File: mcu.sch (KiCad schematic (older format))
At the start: 15 parts, among them U17 STM32F407VETx, Y1 Crystal_Small

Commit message: Transformation will begin shortly... ;-)
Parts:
- added C17: 100n, Capacitors_SMD:C_1206_HandSoldering, symbol C_Small
- added D5: LED.RED, LEDs:LED_1206, symbol Led_Small
- added J1: Micro_SD_Card_Det, RetroBitLab:microSD_HC_Hirose_DM3D-SF, symbol Micro_SD_Card_Det
- added R10, R20: 220, Resistors_SMD:R_1206_HandSoldering, symbol R_Small
- added R11, R12: 10k, Resistors_SMD:R_1206_HandSoldering, symbol R_Small
- added R13, R14, R15, R16, R17, R19: 0, Resistors_SMD:R_1206_HandSoldering, symbol R_Small
- added R18: 47k, Resistors_SMD:R_1206_HandSoldering, symbol R_Small
- C14, C15, C16, C6, C7, C8, C9: footprint (none) -> Capacitors_SMD:C_1206_HandSoldering
- C4, C5: value C_Small -> 20p; footprint (none) -> Capacitors_SMD:C_1206_HandSoldering
- D3: value Led_Small -> LED.GREEN; footprint (none) -> LEDs:LED_1206
- D4: value Led_Small -> LED.AMBER; footprint (none) -> LEDs:LED_1206
- R4, R5: footprint (none) -> Resistors_SMD:R_1206_HandSoldering
- U17: footprint Package_QFP:LQFP-100_14x14mm_P0.5mm -> Housings_QFP:LQFP-100_14x14mm_Pitch0.5mm
- Y1: value Crystal_Small -> 8Mhz; footprint (none) -> Crystal:Crystal_SMD_0603-4Pin_6.0x3.5mm_HandSoldering
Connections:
- net GND: now also C17.2, D5.1 (K), J1.6 (VSS), R13.1, R14.1, R15.1, R16.1, R17.1
- net VCC3V3: now also C17.1, J1.4 (VDD), R11.1, R12.1, R18.1
- net mSDCLK: now also J1.5 (CLK)
- net mSDI: now also J1.3 (CMD)
- net mSDO: now also J1.7 (DAT0), R18.2
- net mD1E0_A10: now reaches U17.1 (PE2)
- net at C4.1, Y1.1: now also R19.2; no longer U17.12 (PH0)
- net at C5.1, Y1.2: now also R20.2; no longer U17.13 (PH1)
- net TP1: now reaches U17.18 (PC3)
- net mD1E0_A11: now reaches U17.2 (PE3)
- net mD1E0_A12: now reaches U17.3 (PE4)
- net LEDGRN: now reaches R4.2, U17.35 (PB0)
- net LEDAMBER: now reaches R5.2
- net LEDAMBER: now also U17.89 (PB3); no longer U17.36 (PB1)
- net mD1E0_A15: now reaches U17.38 (PE7)
- net mD1E0_A13: now reaches U17.4 (PE5)
- net SPARE1: now reaches U17.47 (PB10)
- net SPARE1: now also R13.2
- net SPARE2: now reaches U17.48 (PB11)
- net SPARE2: now also R14.2
- net mD1E0_A14: now reaches U17.5 (PE6)
- net SPARE3: now reaches U17.51 (PB12)
- net SPARE3: now also R15.2
- net SPARE4: now reaches U17.63 (PC6)
- net SPARE4: now also R16.2
- net SPARE5: now reaches U17.64 (PC7)
- net SPARE5: now also R17.2
- net mD1E2_A16: now reaches U17.65 (PC8)
- net mD1E2_A17: now reaches U17.66 (PC9)
- net ~mIRQ: now reaches U17.67 (PA8)
- net UART_TX_TTL: now reaches U17.68 (PA9)
- net UART_TX_TTL: now also R12.2
- net UART_RX_TTL: now reaches U17.69 (PA10)
- net UART_RX_TTL: now also R11.2
- net mD1E3_A21: now reaches U17.7 (PC13)
- net ~mREF: now reaches U17.70 (PA11)
- net ~mD3XX: now reaches U17.71 (PA12)
- net SWDIO: now reaches U17.72 (PA13)
- net SWDCLK: now reaches U17.76 (PA14)
- net RAMEN: now reaches U17.77 (PA15)
- net mD1E2_A18: now reaches U17.78 (PC10)
- net mD1E2_A19: now reaches U17.79 (PC11)
- net mD1E3_A20: now reaches U17.80 (PC12)
- net mRD4: now reaches U17.90 (PB4)
- net mD1E0_A8: now reaches U17.97 (PE0)
- net mD1E0_A9: now reaches U17.98 (PE1)
- net mBO2/PHI2 renamed mB02/PHI2
- net nRST renamed nRESET
- new net: R19.1, U17.12 (PH0)
- new net: R20.1, U17.13 (PH1)
- new net: D5.2 (A), R10.1
- new net LEDRED: R10.2, U17.36 (PB1)
- no-connect marks 3 -> 19
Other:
- note added: "AMBER LED (MEMORY ACCESS SRAM)"
- note added: "GREEN LED (CARTRIDGE SWITCHING)"
- note added: "MICROSD Card Connector in SPI MODE"
- note added: "RED LED (BOARD OK)"
- moved on the sheet: D3, D4, R4, R5

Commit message: Heavily modified. Now it sports a 1024/2048k MIO Ram Expansion and a UNO Cart
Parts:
- renumbered C17 to C10, C6 to C11, C7 to C12, C8 to C13, C9 to C14, C14 to C15, C15 to C16, C16 to C17, C4 to C8, C5 to C9, D5 to D4, D4 to D5, R18 to R10, R4 to R18, R10 to R19, R5 to R20, R19 to R8, R20 to R9, Y1 to XT1
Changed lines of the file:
@@
 VCC3V3
 $Comp
-L Crystal_Small Y1
+L Crystal_Small XT1
 U 1 1 5C421B52
 P 2500 2700
-F 0 "Y1" H 2500 2800 50  0000 C CNN
+F 0 "XT1" H 2500 2800 50  0000 C CNN
 F 1 "8Mhz" H 2500 2600 50  0000 C CNN
 F 2 "Crystal:Crystal_SMD_0603-4Pin_6.0x3.5mm_HandSoldering" H 2500 2700 50  0001 C CNN
@@
 $EndComp
 $Comp
-L C_Small C4
+L C_Small C8
 U 1 1 5C421C91
 P 2100 2350
-F 0 "C4" H 2110 2420 50  0000 L CNN
+F 0 "C8" H 2110 2420 50  0000 L CNN
 F 1 "20p" H 2110 2270 50  0000 L CNN
 F 2 "Capacitors_SMD:C_1206_HandSoldering" H 2100 2350 50  0001 C CNN
@@
 $EndComp
 $Comp
-L C_Small C5
+L C_Small C9
 U 1 1 5C421D1B
 P 2100 3050
-F 0 "C5" H 2110 3120 50  0000 L CNN
+F 0 "C9" H 2110 3120 50  0000 L CNN
 F 1 "20p" H 2110 2970 50  0000 L CNN
 F 2 "Capacitors_SMD:C_1206_HandSoldering" H 2100 3050 50  0001 C CNN
@@
 $EndComp
 $Comp
-L C_Small C6
+L C_Small C11
 U 1 1 5C421E29
 P 8600 850
-F 0 "C6" H 8610 920 50  0000 L CNN
+F 0 "C11" H 8610 920 50  0000 L CNN
 F 1 "100n" H 8610 770 50  0000 L CNN
 F 2 "Capacitors_SMD:C_1206_HandSoldering" H 8600 850 50  0001 C CNN
@@
 $EndComp
 $Comp
-L C_Small C7
+L C_Small C12
 U 1 1 5C421EE5
 P 8600 1200
-F 0 "C7" H 8610 1270 50  0000 L CNN
+F 0 "C12" H 8610 1270 50  0000 L CNN
 F 1 "100n" H 8610 1120 50  0000 L CNN
 F 2 "Capacitors_SMD:C_1206_HandSoldering" H 8600 1200 50  0001 C CNN
@@
 $EndComp
 $Comp
-L C_Small C8
+L C_Small C13
 U 1 1 5C421F19
 P 8600 1550
-F 0 "C8" H 8610 1620 50  0000 L CNN
+F 0 "C13" H 8610 1620 50  0000 L CNN
 F 1 "100n" H 8610 1470 50  0000 L CNN
 F 2 "Capacitors_SMD:C_1206_HandSoldering" H 8600 1550 50  0001 C CNN
@@
 $EndComp
 $Comp
-L C_Small C9
+L C_Small C14
 U 1 1 5C421F4C
 P 8600 1900
-F 0 "C9" H 8610 1970 50  0000 L CNN
+F 0 "C14" H 8610 1970 50  0000 L CNN
 F 1 "100n" H 8610 1820 50  0000 L CNN
 F 2 "Capacitors_SMD:C_1206_HandSoldering" H 8600 1900 50  0001 C CNN
@@
 $EndComp
 $Comp
-L C_Small C14
+L C_Small C15
 U 1 1 5C421F82
 P 8600 2250
-F 0 "C14" H 8610 2320 50  0000 L CNN
+F 0 "C15" H 8610 2320 50  0000 L CNN
 F 1 "100n" H 8610 2170 50  0000 L CNN
 F 2 "Capacitors_SMD:C_1206_HandSoldering" H 8600 2250 50  0001 C CNN
@@
 $EndComp
 $Comp
-L C_Small C15
+L C_Small C16
 U 1 1 5C421FB7
 P 8600 2600
-F 0 "C15" H 8610 2670 50  0000 L CNN
+F 0 "C16" H 8610 2670 50  0000 L CNN
 F 1 "100n" H 8610 2520 50  0000 L CNN
 F 2 "Capacitors_SMD:C_1206_HandSoldering" H 8600 2600 50  0001 C CNN
@@
 $EndComp
 $Comp
-L C_Small C16
+L C_Small C17
 U 1 1 5C421FF7
 P 8600 2950
-F 0 "C16" H 8610 3020 50  0000 L CNN
+F 0 "C17" H 8610 3020 50  0000 L CNN
 F 1 "100n" H 8610 2870 50  0000 L CNN
 F 2 "Capacitors_SMD:C_1206_HandSoldering" H 8600 2950 50  0001 C CNN
@@
 ~mD1XX
 $Comp
-L R_Small R4
+L R_Small R18
 U 1 1 5C422FC6
 P 9950 3850
-F 0 "R4" H 9980 3870 50  0000 L CNN
+F 0 "R18" H 9980 3870 50  0000 L CNN
 F 1 "220" H 9980 3810 50  0000 L CNN
 F 2 "Resistors_SMD:R_1206_HandSoldering" H 9950 3850 50  0001 C CNN
@@
 $EndComp
 $Comp
-L R_Small R5
+L R_Small R20
 U 1 1 5C42306F
 P 10650 3850
-F 0 "R5" H 10680 3870 50  0000 L CNN
+F 0 "R20" H 10680 3870 50  0000 L CNN
 F 1 "220" H 10680 3810 50  0000 L CNN
 F 2 "Resistors_SMD:R_1206_HandSoldering" H 10650 3850 50  0001 C CNN
@@
 $EndComp
 $Comp
-L Led_Small D4
+L Led_Small D5
 U 1 1 5C4231C2
 P 10650 3650
-F 0 "D4" H 10600 3775 50  0000 L CNN
+F 0 "D5" H 10600 3775 50  0000 L CNN
 F 1 "LED.AMBER" H 10475 3550 50  0000 L CNN
 F 2 "LEDs:LED_1206" V 10650 3650 50  0001 C CNN
@@
 mRD4
 $Comp
-L R_Small R10
+L R_Small R19
 U 1 1 5C4340D0
 P 10300 3850
-F 0 "R10" H 10330 3870 50  0000 L CNN
+F 0 "R19" H 10330 3870 50  0000 L CNN
 F 1 "220" H 10330 3810 50  0000 L CNN
 F 2 "Resistors_SMD:R_1206_HandSoldering" H 10300 3850 50  0001 C CNN
@@
 $EndComp
 $Comp
-L Led_Small D5
+L Led_Small D4
 U 1 1 5C4340D8
 P 10300 3650
-F 0 "D5" H 10250 3775 50  0000 L CNN
+F 0 "D4" H 10250 3775 50  0000 L CNN
 F 1 "LED.RED" H 10125 3550 50  0000 L CNN
 F 2 "LEDs:LED_1206" V 10300 3650 50  0001 C CNN
@@
 mSDI
 $Comp
-L R_Small R18
+L R_Small R10
 U 1 1 5C4392C7
 P 2900 4250
-F 0 "R18" H 2700 4250 50  0000 L CNN
+F 0 "R10" H 2700 4250 50  0000 L CNN
 F 1 "47k" H 2950 4250 50  0000 L CNN
 F 2 "Resistors_SMD:R_1206_HandSoldering" H 2900 4250 50  0001 C CNN
@@
 	2400 4450 3150 4450
 $Comp
-L C_Small C17
+L C_Small C10
 U 1 1 5C43AFC5
 P 3500 4950
-F 0 "C17" H 3510 5020 50  0000 L CNN
+F 0 "C10" H 3510 5020 50  0000 L CNN
 F 1 "100n" H 3510 4870 50  0000 L CNN
 F 2 "Capacitors_SMD:C_1206_HandSoldering" H 3500 4950 50  0001 C CNN
@@
 ~mIRQ
 $Comp
-L R_Small R20
+L R_Small R9
 U 1 1 5C43FC39
 P 2850 3050
-F 0 "R20" H 2880 3070 50  0000 L CNN
+F 0 "R9" H 2880 3070 50  0000 L CNN
 F 1 "220" H 2880 3010 50  0000 L CNN
 F 2 "Resistors_SMD:R_1206_HandSoldering" H 2850 3050 50  0001 C CNN
@@
 $EndComp
 $Comp
-L R_Small R19
+L R_Small R8
 U 1 1 5C43FCB0
 P 2850 2350
-F 0 "R19" H 2880 2370 50  0000 L CNN
+F 0 "R8" H 2880 2370 50  0000 L CNN
 F 1 "0" H 2880 2310 50  0000 L CNN
 F 2 "Resistors_SMD:R_1206_HandSoldering" H 2850 2350 50  0001 C CNN

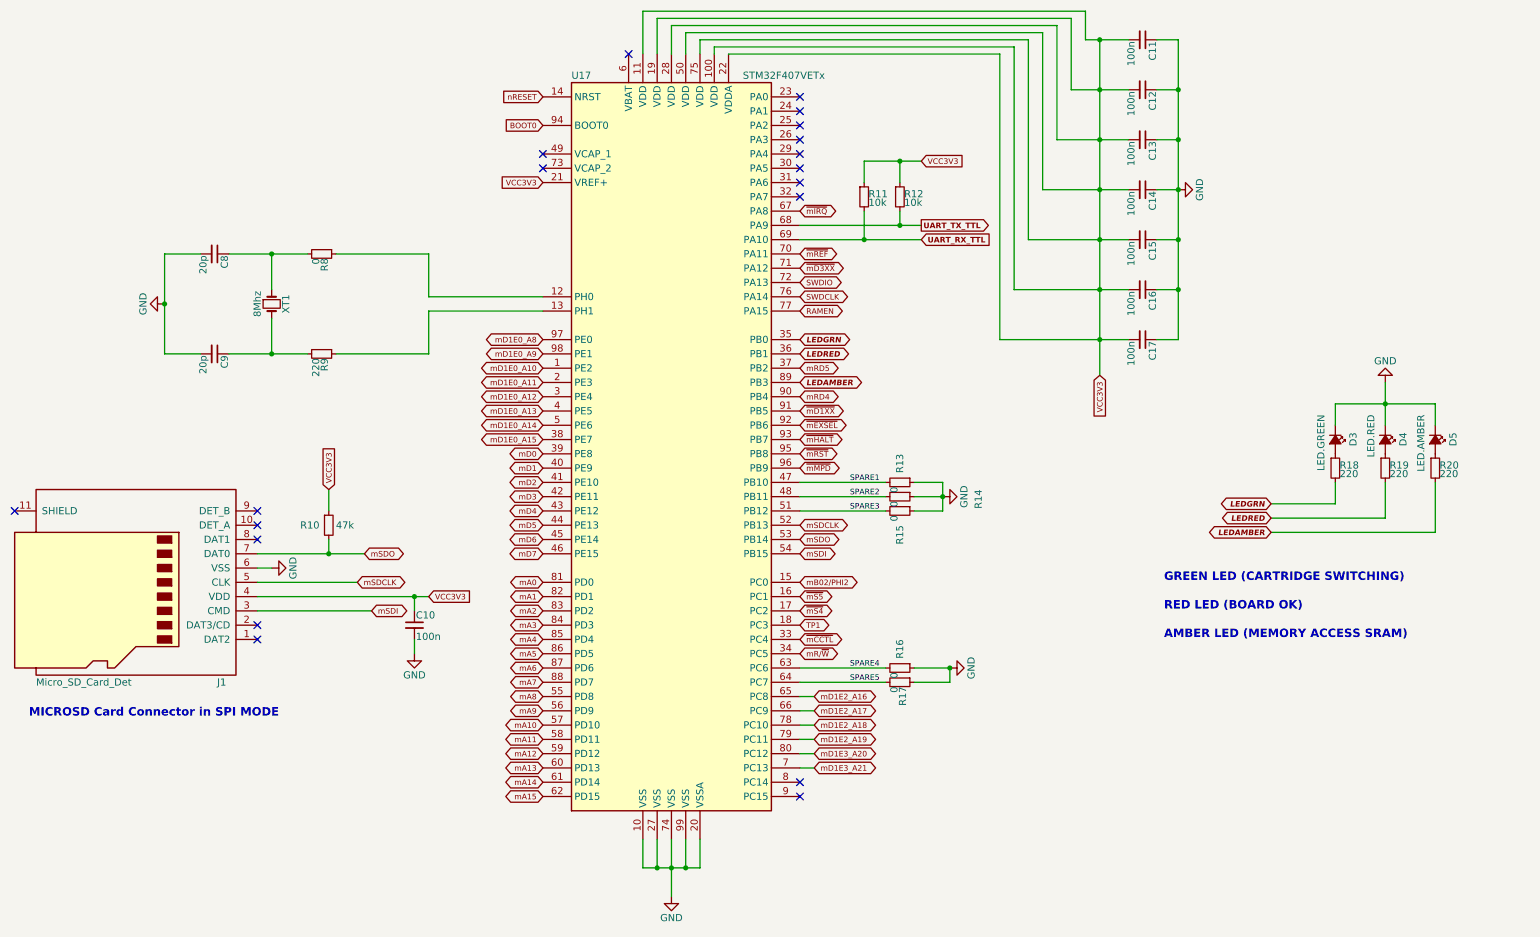
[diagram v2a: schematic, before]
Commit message: Upgraded with the latest infos
Now there is no logic for address/decoding. All is done inside the
microprocessor. This is a semi-final release.
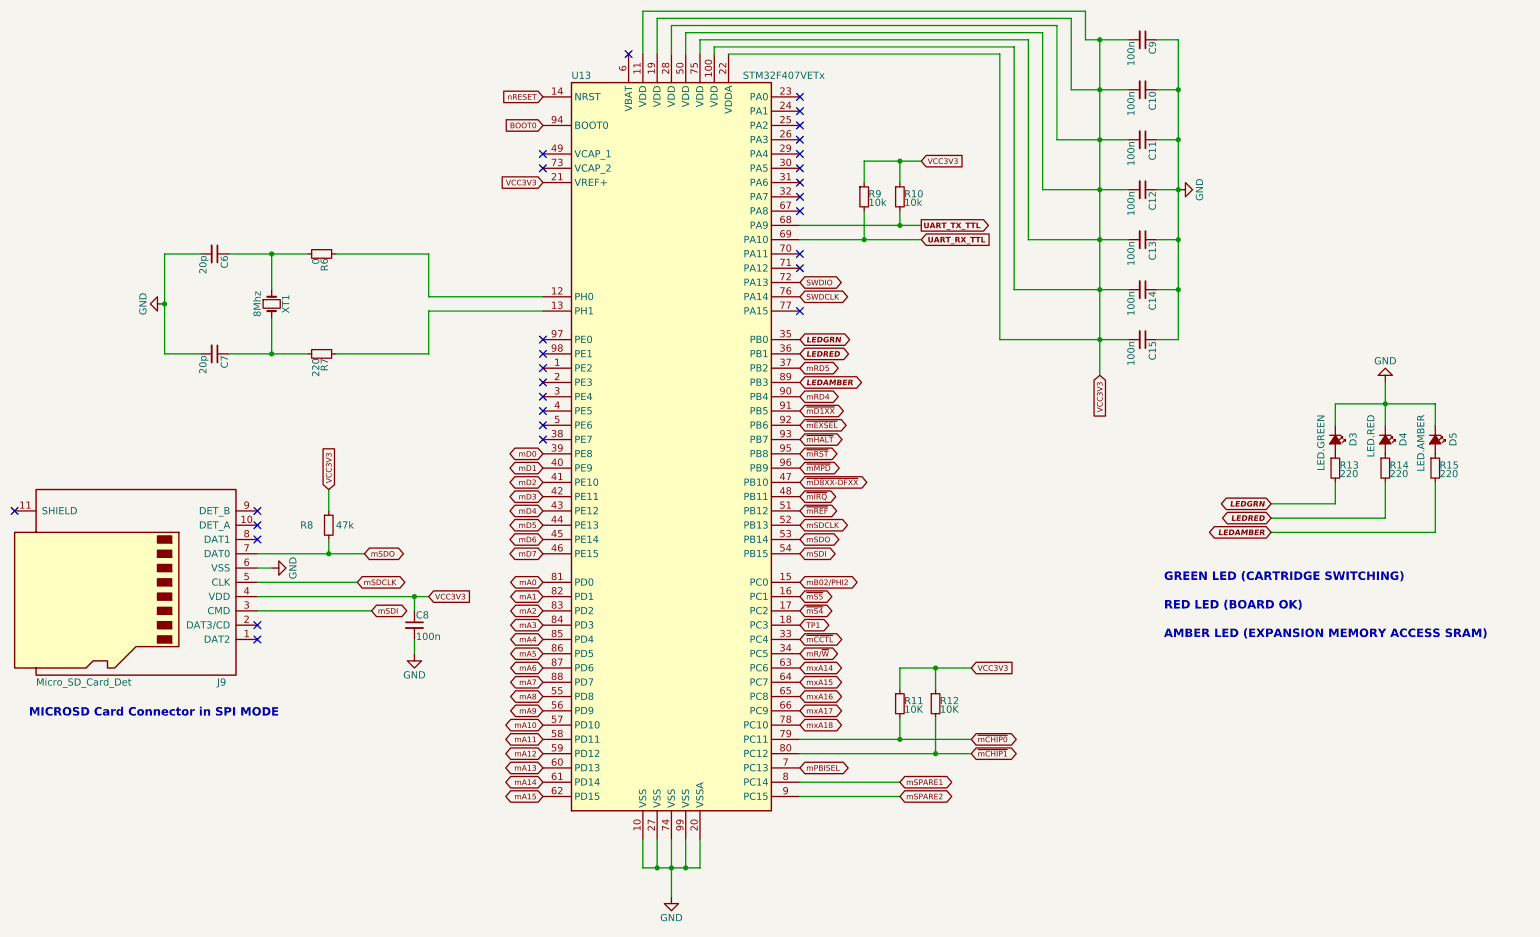
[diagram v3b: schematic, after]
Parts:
- removed R13, R14, R15, R16, R17: 0, Resistors_SMD:R_1206_HandSoldering, symbol R_Small
- added R11, R12: 10K, Resistors_SMD:R_1206_HandSoldering, symbol R_Small
- renumbered C12 to C10, C13 to C11, C14 to C12, C15 to C13, C16 to C14, C17 to C15, C8 to C6, C9 to C7, C10 to C8, C11 to C9, J1 to J9, R12 to R10, R18 to R13, R19 to R14, R20 to R15, R8 to R6, R9 to R7, R10 to R8, R11 to R9, U17 to U13
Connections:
- net SPARE2 is gone; now on net ~mIRQ: U13.48 (PB11)
- net SPARE3 is gone; now on net ~mREF: U13.51 (PB12)
- net VCC3V3: now also R11.1, R12.1
- net ~mIRQ: no longer U13.67 (PA8)
- net ~mREF: no longer U13.70 (PA11)
- net mSPARE1: now reaches U13.8 (PC14)
- net mSPARE2: now reaches U13.9 (PC15)
- net RAMEN: no longer names the net of U13.77 (PA15)
- net SPARE1 renamed ~mD8XX-DFXX
- net SPARE4 renamed mxA14
- net SPARE5 renamed mxA15
- net mD1E0_A10: no longer names the net of U13.1 (PE2)
- net mD1E0_A11: no longer names the net of U13.2 (PE3)
- net mD1E0_A12: no longer names the net of U13.3 (PE4)
- net mD1E0_A13: no longer names the net of U13.4 (PE5)
- net mD1E0_A14: no longer names the net of U13.5 (PE6)
- net mD1E0_A15: no longer names the net of U13.38 (PE7)
- net mD1E0_A8: no longer names the net of U13.97 (PE0)
- net mD1E0_A9: no longer names the net of U13.98 (PE1)
- net mD1E2_A16 renamed mxA16
- net mD1E2_A17 renamed mxA17
- net mD1E2_A18 renamed mxA18
- net mD1E2_A19 renamed ~mCHIP0
- net ~mCHIP0: now also R11.2
- net mD1E3_A20 renamed ~mCHIP1
- net ~mCHIP1: now also R12.2
- net mD1E3_A21 renamed mPBISEL
- net ~mD3XX: no longer names the net of U13.71 (PA12)
- no-connect marks 19 -> 29
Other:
- note added: "AMBER LED (EXPANSION MEMORY ACCESS SRAM)"
- note removed: "AMBER LED (MEMORY ACCESS SRAM)"

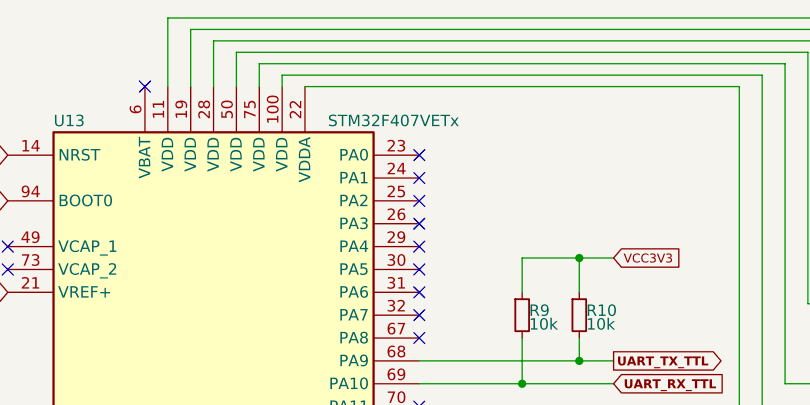
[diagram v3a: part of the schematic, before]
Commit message: Changed Housing for STM32F407VGTx
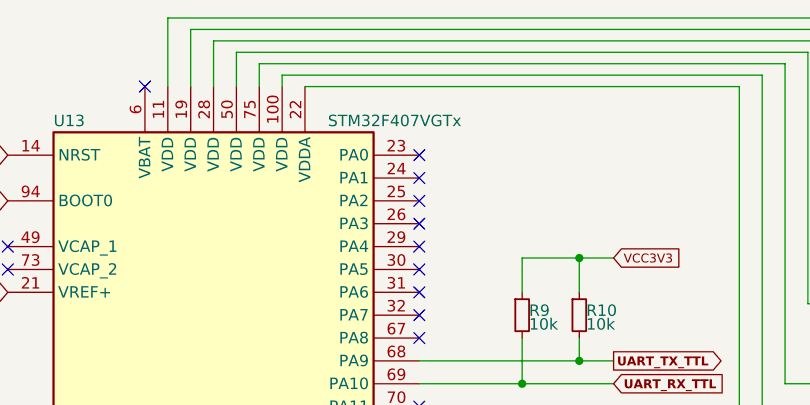
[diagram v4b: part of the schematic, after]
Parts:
- removed U13: STM32F407VETx, Housings_QFP:LQFP-100_14x14mm_Pitch0.5mm, symbol STM32F407VETx
- added U13: STM32F407VGTx, Housings_QFP:TQFP-100_14x14mm_Pitch0.5mm, symbol STM32F407VGTx
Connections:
- net BOOT0: now also U13.94 (BOOT0)
- net GND: now also U13.10 (VSS), U13.20 (VSSA), U13.27 (VSS), U13.74 (VSS), U13.99 (VSS)
- net LEDAMBER: now also U13.89 (PB3)
- net LEDGRN: now also U13.35 (PB0)
- net LEDRED: now also U13.36 (PB1)
- net SWDCLK: now also U13.76 (PA14)
- net SWDIO: now also U13.72 (PA13)
- net TP1: now also U13.18 (PC3)
- net UART_RX_TTL: now also U13.69 (PA10)
- net UART_TX_TTL: now also U13.68 (PA9)
- net VCC3V3: now also U13.100 (VDD), U13.11 (VDD), U13.19 (VDD), U13.21 (VREF+), U13.22 (VDDA), U13.28 (VDD), U13.50 (VDD), U13.75 (VDD)
- net mA0: now also U13.81 (PD0)
- net mA1: now also U13.82 (PD1)
- net mA10: now also U13.57 (PD10)
- net mA11: now also U13.58 (PD11)
- net mA12: now also U13.59 (PD12)
- net mA13: now also U13.60 (PD13)
- net mA14: now also U13.61 (PD14)
- net mA15: now also U13.62 (PD15)
- net mA2: now also U13.83 (PD2)
- net mA3: now also U13.84 (PD3)
- net mA4: now also U13.85 (PD4)
- net mA5: now also U13.86 (PD5)
- net mA6: now also U13.87 (PD6)
- net mA7: now also U13.88 (PD7)
- net mA8: now also U13.55 (PD8)
- net mA9: now also U13.56 (PD9)
- net mB02/PHI2: now also U13.15 (PC0)
- net mD0: now also U13.39 (PE8)
- net mD1: now also U13.40 (PE9)
- net mD2: now also U13.41 (PE10)
- net mD3: now also U13.42 (PE11)
- net mD4: now also U13.43 (PE12)
- net mD5: now also U13.44 (PE13)
- net mD6: now also U13.45 (PE14)
- net mD7: now also U13.46 (PE15)
- net mPBISEL: now also U13.7 (PC13)
- net mR/~W: now also U13.34 (PC5)
- net mRD4: now also U13.90 (PB4)
- net mRD5: now also U13.37 (PB2)
- net mSDCLK: now also U13.52 (PB13)
- net mSDI: now also U13.54 (PB15)
- net mSDO: now also U13.53 (PB14)
- net mSPARE1: now also U13.8 (PC14)
- net mSPARE2: now also U13.9 (PC15)
- net mxA14: now also U13.63 (PC6)
- net mxA15: now also U13.64 (PC7)
- net mxA16: now also U13.65 (PC8)
- net mxA17: now also U13.66 (PC9)
- net mxA18: now also U13.78 (PC10)
- net nRESET: now also U13.14 (NRST)
- net ~mCCTL: now also U13.33 (PC4)
- net ~mCHIP0: now also U13.79 (PC11)
- net ~mCHIP1: now also U13.80 (PC12)
- net ~mD1XX: now also U13.91 (PB5)
- net ~mD8XX-DFXX: now also U13.47 (PB10)
- net ~mEXSEL: now also U13.92 (PB6)
- net ~mHALT: now also U13.93 (PB7)
- net ~mIRQ: now also U13.48 (PB11)
- net ~mMPD: now also U13.96 (PB9)
- net ~mREF: now also U13.51 (PB12)
- net ~mRST: now also U13.95 (PB8)
- net ~mS4: now also U13.17 (PC2)
- net ~mS5: now also U13.16 (PC1)
- net at R6.1: now also U13.12 (PH0)
- net at R7.1: now also U13.13 (PH1)
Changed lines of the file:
@@
 Comment4 ""
 $EndDescr
-$Comp
-L STM32F407VETx U13
-U 1 1 5C42189F
-P 5300 3650
-F 0 "U13" H 4600 6200 50  0000 L CNN
-F 1 "STM32F407VETx" H 5800 6200 50  0000 L CNN
-F 2 "Housings_QFP:LQFP-100_14x14mm_Pitch0.5mm" H 4600 1050 50  0001 R CNN
-F 3 "" H 5300 3650 50  0001 C CNN
-	1    5300 3650
-	1    0    0    -1
-$EndComp
 NoConn ~ 5000 950
 Text GLabel 4400 1250 0    39   Input ~ 0
@@
 Text GLabel 6200 4150 2    39   BiDi ~ 0
 ~mREF
+$Comp
+L STM32F407VGTx U13
+U 1 1 5C61E27E
+P 5300 3650
+F 0 "U13" H 4600 6200 50  0000 L CNN
+F 1 "STM32F407VGTx" H 5800 6200 50  0000 L CNN
+F 2 "Housings_QFP:TQFP-100_14x14mm_Pitch0.5mm" H 4600 1050 50  0001 R CNN
+F 3 "" H 5300 3650 50  0001 C CNN
+	1    5300 3650
+	1    0    0    -1
+$EndComp
 $EndSCHEMATC
